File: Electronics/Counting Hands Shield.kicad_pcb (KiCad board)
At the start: 2 copper layers, 62.2 x 57.2 mm, 29 parts, among them P1 Arduino P0-P7, P10 Servo_3, P11 Servo_4, P12 Servo_5, P2 Arduino P8-SCL, P3 Arduino A5-A0, P4 Arduino Vin-Blank, P5 LEDs Anodes, P6 LEDs Cat, P7 Servo_H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

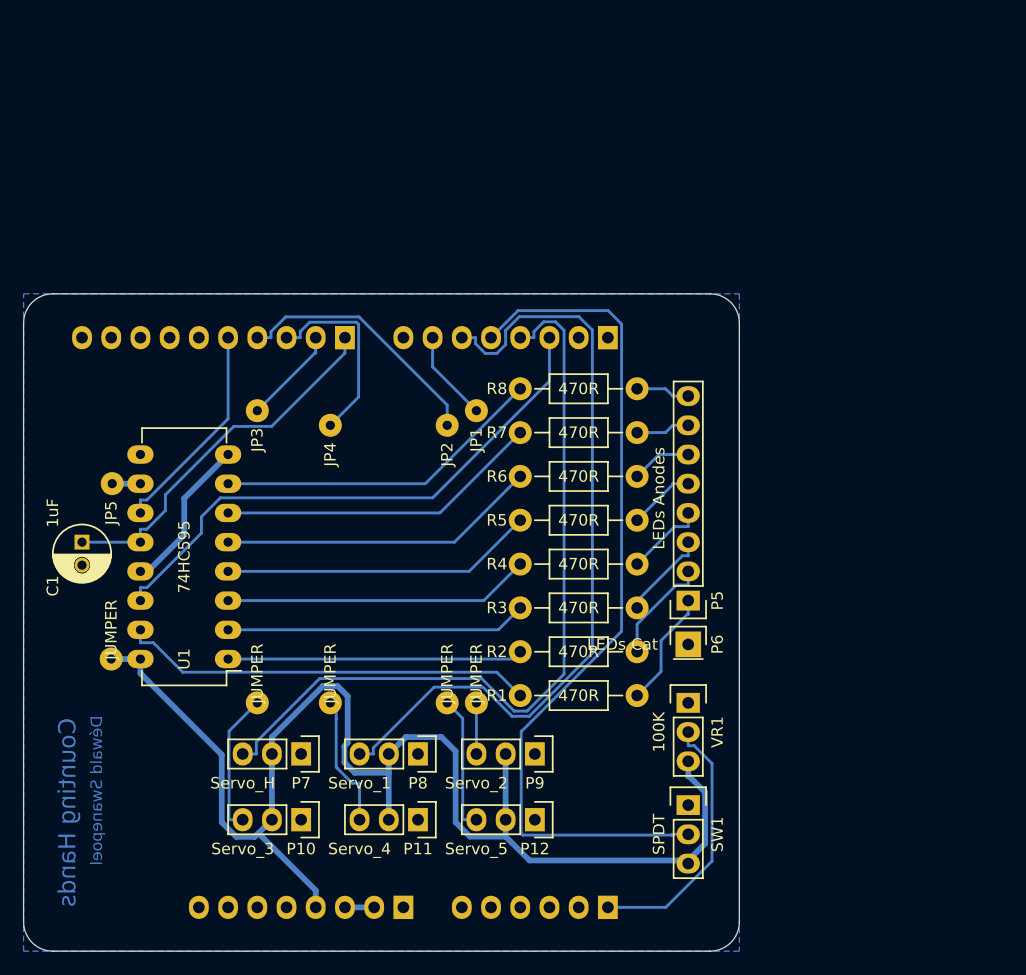
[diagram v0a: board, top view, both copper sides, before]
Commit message: Changes to KiCAD project
Replaced Potentiometer (VR1) with Rotary Encoder (P6)

Added 2DIP switch for default interval

Replaced 8 LEDs progress indicator and 74HC595 Shift Register with 4 digit 7 Segment Display
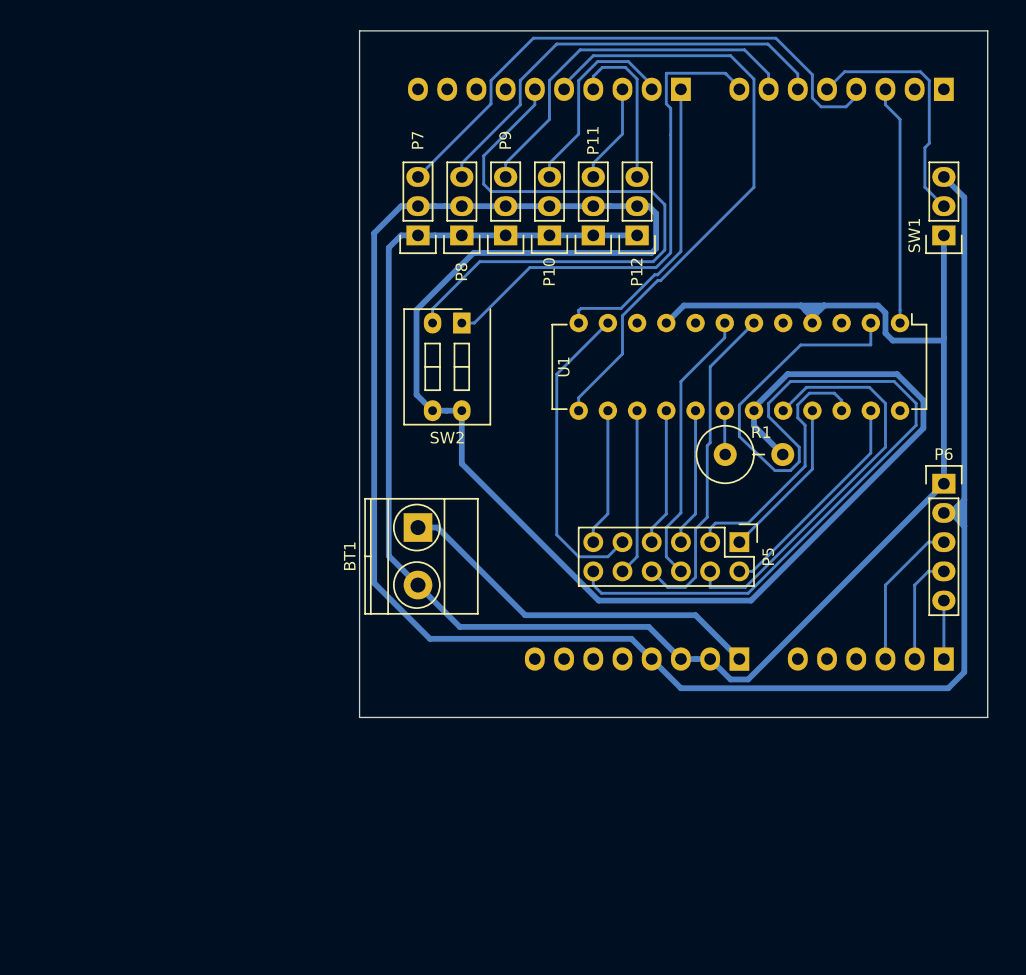
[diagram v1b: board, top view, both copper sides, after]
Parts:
- removed C1: 1uF, Capacitors_ThroughHole:C_Radial_D5_L11_P2
- removed JP1, JP2, JP3, JP4, JP5: JUMPER, Personal:Jumper
- removed R2, R3, R4, R5, R6, R7, R8: 470R, Resistors_ThroughHole:Resistor_Horizontal_RM10mm
- removed VR1: 100K, Pin_Headers:Pin_Header_Straight_1x03
- added BT1: 7-12V, Terminal_Blocks:TerminalBlock_Pheonix_MKDS1.5-2pol, F.Cu at (119.4, 104.1)
- added SW2: Default Interval, Buttons_Switches_ThroughHole:SW_DIP_x2_Slide, F.Cu at (123.2, 86.4)
- P5: value LEDs Anodes -> 4 Digit 7 Segment Display; footprint Pin_Headers:Pin_Header_Straight_1x08 -> Pin_Headers:Pin_Header_Straight_2x06
- P6: value LEDs Cat -> Rotary; footprint Pin_Headers:Pin_Header_Straight_1x01 -> Pin_Headers:Pin_Header_Straight_1x05
- R1: value 470R -> 10K; footprint Resistors_ThroughHole:Resistor_Horizontal_RM10mm -> Resistors_ThroughHole:Resistor_Vertical_RM5mm
- SW1: value SPDT -> Direction
- U1: value 74HC595 -> MAX7219; footprint Housings_DIP:DIP-16_W7.62mm_LongPads -> Housings_DIP:DIP-24_W7.62mm
- moved U1 65.3 mm to (161.3, 86.4), turned to 270 degrees
- moved P10 55.2 mm to (130.8, 78.7), turned to 180 degrees
- moved SW1 54.3 mm to (165.1, 78.7), turned to 180 degrees
- moved P11 53.0 mm to (134.6, 78.7), turned to 180 degrees
- moved P12 51.6 mm to (138.4, 78.7), turned to 180 degrees
- moved P7 46.2 mm to (119.4, 78.7), turned to 180 degrees
- moved P8 45.2 mm to (123.2, 78.7), turned to 180 degrees
- moved P9 45.2 mm to (127.0, 78.7), turned to 180 degrees
- moved P3 36.3 mm to (165.1, 115.6)
- moved P1 36.3 mm to (165.1, 66.0)
- moved P2 36.3 mm to (142.2, 66.0)
- moved P4 36.3 mm to (147.3, 115.6)
- moved P6 26.3 mm to (165.1, 100.3)
- moved R1 23.3 mm to (148.6, 97.8), turned to 0 degrees
- moved P5 6.75 mm to (147.3, 105.4), turned to 270 degrees
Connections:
- P1 pad 7: Net-(JP1-Pad1) -> Net-(P1-Pad7)
- P1 pad 8: (no net) -> Net-(P1-Pad8)
- P10 pad 1: GND -> /GND
- P10 pad 3: Net-(JP3-Pad2) -> Net-(P10-Pad3)
- P11 pad 1: GND -> /GND
- P11 pad 3: Net-(JP4-Pad2) -> Net-(P11-Pad3)
- P12 pad 1: GND -> /GND
- P12 pad 3: Net-(JP2-Pad2) -> Net-(P12-Pad3)
- P2 pad 2: Net-(JP3-Pad1) -> Net-(P10-Pad3)
- P2 pad 3: Net-(JP4-Pad1) -> Net-(P11-Pad3)
- P2 pad 4: Net-(JP2-Pad1) -> Net-(P12-Pad3)
- P2 pad 6: (no net) -> Net-(P2-Pad6)
- P3 pad 2: (no net) -> Net-(P3-Pad2)
- P3 pad 3: (no net) -> Net-(P3-Pad3)
- P4 pad 1: (no net) -> /Vin
- P4 pad 2: GND -> /GND
- P4 pad 3: GND -> /GND
- P6 pad 1: GND -> /GND
- P7 pad 1: GND -> /GND
- P8 pad 1: GND -> /GND
- P9 pad 1: GND -> /GND
- P9 pad 3: Net-(JP1-Pad2) -> Net-(P1-Pad7)
- R1 pad 1: Net-(P5-Pad1) -> Net-(R1-Pad1)
- R1 pad 2: Net-(R1-Pad2) -> VCC
- SW1 pad 1: GND -> /GND
- U1 pad 1: Net-(R2-Pad2) -> Net-(P1-Pad3)
- U1 pad 10: Net-(JP5-Pad2) -> (no net)
- U1 pad 11: Net-(P2-Pad5) -> Net-(P5-Pad9)
- U1 pad 13: GND -> Net-(P2-Pad5)
- U1 pad 14: Net-(P1-Pad3) -> Net-(P5-Pad11)
- U1 pad 15: Net-(R1-Pad2) -> Net-(P5-Pad10)
- U1 pad 16: VCC -> Net-(P5-Pad7)
- U1 pad 2: Net-(R3-Pad2) -> Net-(P5-Pad12)
- U1 pad 3: Net-(R4-Pad1) -> (no net)
- U1 pad 4: Net-(R5-Pad1) -> /GND
- U1 pad 5: Net-(R6-Pad1) -> (no net)
- U1 pad 6: Net-(R7-Pad1) -> Net-(P5-Pad8)
- U1 pad 7: Net-(R8-Pad1) -> Net-(P5-Pad6)
- U1 pad 8: GND -> (no net)
- U1 pad 9: (no net) -> /GND
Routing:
- net /GND: track 0.00 -> 163.3 mm
- net VCC: track 118.1 -> 280.8 mm
- net Net-(P5-Pad12): track 0.00 -> 83.0 mm
- net Net-(P2-Pad6): track 0.00 -> 54.1 mm
- net Net-(P1-Pad5): track 75.3 -> 21.6 mm
- net Net-(P1-Pad8): track 0.00 -> 43.5 mm
- net Net-(R1-Pad2): track 36.0 -> 0.00 mm
- net Net-(P2-Pad5): track 18.7 -> 54.0 mm
- net /Vin: track 0.00 -> 32.7 mm
- net Net-(P1-Pad7): track 0.00 -> 32.3 mm
- net Net-(P1-Pad6): track 69.1 -> 38.3 mm
- net Net-(P5-Pad4): track 6.98 -> 35.8 mm
- net Net-(R8-Pad1): track 28.8 -> 0.00 mm
- net Net-(R7-Pad1): track 28.3 -> 0.00 mm
- net Net-(P1-Pad3): track 48.7 -> 20.8 mm
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- removed copper zone on B.Cu, net GND
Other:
- board size 62.2 x 57.2 mm -> 54.6 x 59.7 mm
- board text removed: "Counting Hands"
- board text removed: "Déwald Swanepoel"

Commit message: Changes to KiCAD project
Tidied up schematic and PCB
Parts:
- removed R1: 10K, Resistors_ThroughHole:Resistor_Vertical_RM5mm
- removed U1: MAX7219, Housings_DIP:DIP-24_W7.62mm
- P5: value 4 Digit 7 Segment Display -> 4x7 Segment Display; footprint Pin_Headers:Pin_Header_Straight_2x06 -> Pin_Headers:Pin_Header_Straight_1x04
- moved P5 32.1 mm to (165.1, 78.7), turned to 180 degrees
- moved SW1 10.2 mm to (165.1, 88.9)
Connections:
- P10 pad 2: VCC -> /5V
- P11 pad 2: VCC -> /5V
- P12 pad 2: VCC -> /5V
- P2 pad 6: Net-(P2-Pad6) -> (no net)
- P4 pad 4: VCC -> /5V
- P5 pad 1: Net-(P5-Pad1) -> /GND
- P5 pad 2: Net-(P5-Pad2) -> /5V
- P5 pad 3: Net-(P5-Pad3) -> Net-(P1-Pad3)
- P5 pad 4: Net-(P5-Pad4) -> Net-(P2-Pad5)
- P6 pad 2: VCC -> /5V
- P7 pad 2: VCC -> /5V
- P8 pad 2: VCC -> /5V
- P9 pad 2: VCC -> /5V
- SW1 pad 3: VCC -> /5V
- SW2 pad 2: Net-(P2-Pad6) -> Net-(P2-Pad1)
- SW2 pad 3: VCC -> /5V
- SW2 pad 4: VCC -> /5V
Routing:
- net VCC: track 280.8 -> 0.00 mm
- net /5V: track 0.00 -> 224.7 mm
- net Net-(P5-Pad12): track 83.0 -> 0.00 mm
- net Net-(P2-Pad6): track 54.1 -> 0.00 mm
- net Net-(P5-Pad4): track 35.8 -> 0.00 mm
- net Net-(P5-Pad8): track 29.0 -> 0.00 mm
- net Net-(P5-Pad9): track 27.3 -> 0.00 mm
- net Net-(P2-Pad5): track 54.0 -> 80.0 mm
- net /GND: track 163.3 -> 137.5 mm
- net Net-(P5-Pad6): track 24.2 -> 0.00 mm
- net Net-(P5-Pad3): track 22.7 -> 0.00 mm
- net Net-(P5-Pad2): track 19.4 -> 0.00 mm
- net Net-(P5-Pad10): track 14.5 -> 0.00 mm
- net Net-(P5-Pad1): track 14.1 -> 0.00 mm
- net Net-(P5-Pad7): track 12.0 -> 0.00 mm
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- added copper zone on B.Cu, net /5V
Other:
- board size 54.6 x 59.7 mm -> 55.9 x 60.3 mm
- board text added: "Counting Hands v1.0"
- board text added: "Dewald Swanepoel"
